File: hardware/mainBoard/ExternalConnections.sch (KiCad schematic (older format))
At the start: 8 parts

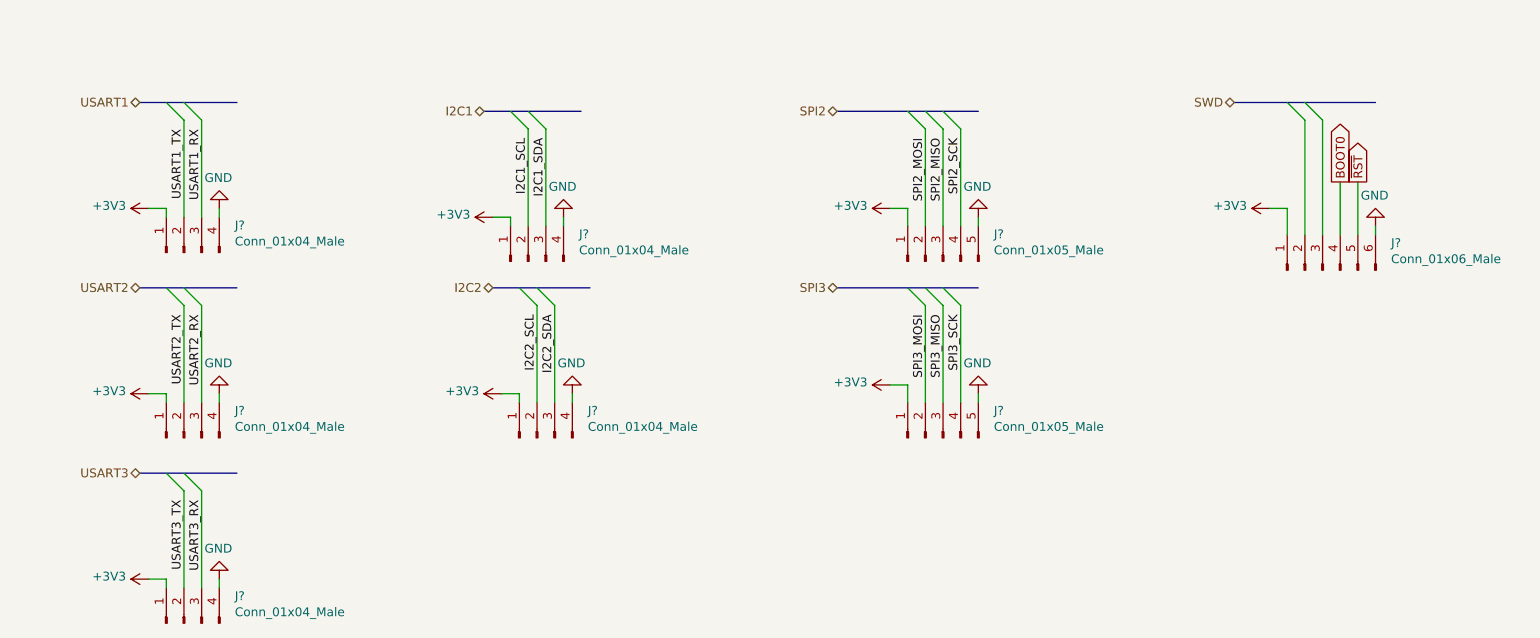
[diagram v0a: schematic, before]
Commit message: Ended schematic, created some pcb footprints
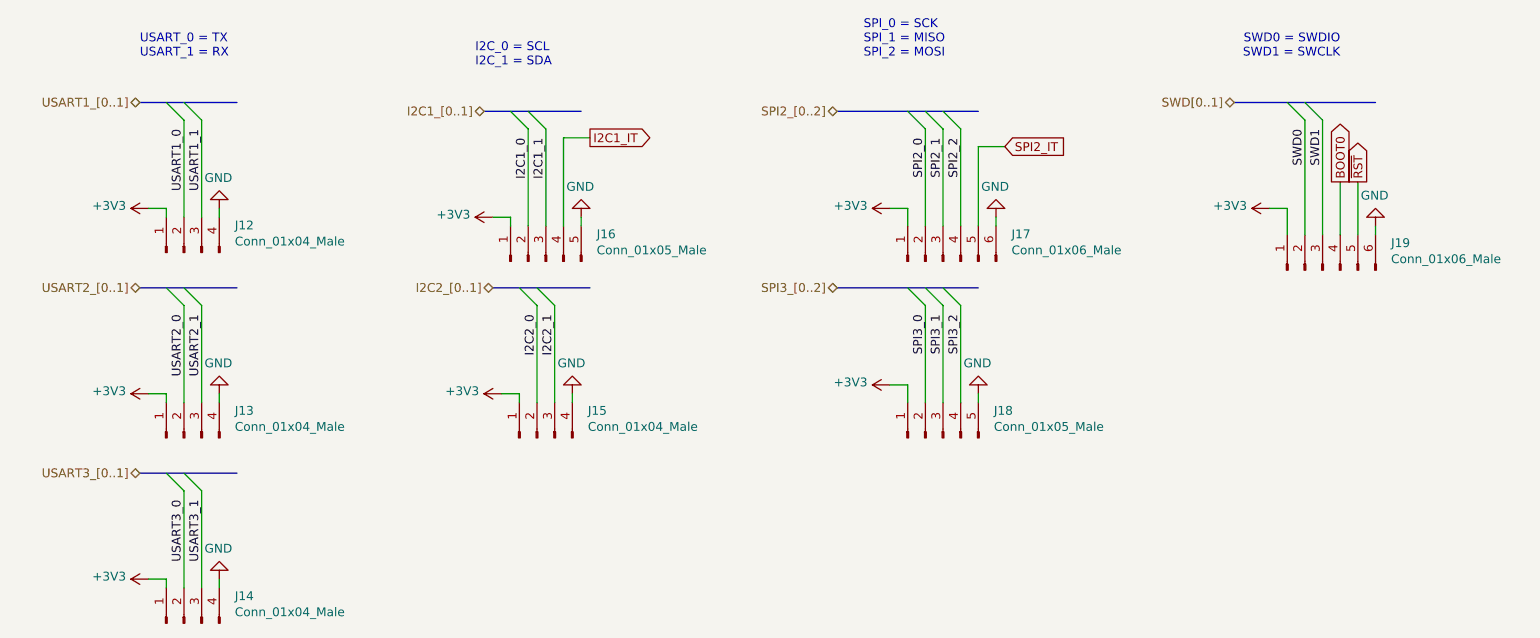
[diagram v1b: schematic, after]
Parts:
- removed J?: Conn_01x04_Male, symbol Connector:Conn_01x04_Male
- removed J?: Conn_01x05_Male, symbol Connector:Conn_01x05_Male
- added J16: Conn_01x05_Male, Connector_JST:JST_EH_B5B-EH-A_1x05_P2.50mm_Vertical, symbol Connector:Conn_01x05_Male
- added J17: Conn_01x06_Male, Connector_JST:JST_EH_B6B-EH-A_1x06_P2.50mm_Vertical, symbol Connector:Conn_01x06_Male
- J12, J13, J14, J15: renamed from J?; footprint (none) -> Connector_JST:JST_EH_B4B-EH-A_1x04_P2.50mm_Vertical
- J18: renamed from J?; footprint (none) -> Connector_JST:JST_EH_B5B-EH-A_1x05_P2.50mm_Vertical
- J19: renamed from J?; footprint (none) -> Connector_JST:JST_EH_B6B-EH-A_1x06_P2.50mm_Vertical
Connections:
- net +3V3: now also J16.1 (Pin_1), J17.1 (Pin_1)
- net GND: now also J16.5 (Pin_5), J17.6 (Pin_6)
- net SWD0: now reaches J19.2 (Pin_2)
- net SWD1: now reaches J19.3 (Pin_3)
- net I2C2_SCL renamed I2C2_0
- net I2C2_SDA renamed I2C2_1
- net SPI3_MISO renamed SPI3_1
- net SPI3_MOSI renamed SPI3_0
- net SPI3_SCK renamed SPI3_2
- net USART1_RX renamed USART1_1
- net USART1_TX renamed USART1_0
- net USART2_RX renamed USART2_1
- net USART2_TX renamed USART2_0
- net USART3_RX renamed USART3_1
- net USART3_TX renamed USART3_0
- new net I2C1_0: J16.2 (Pin_2)
- new net I2C1_1: J16.3 (Pin_3)
- new net I2C1_IT: J16.4 (Pin_4)
- new net SPI2_0: J17.2 (Pin_2)
- new net SPI2_1: J17.3 (Pin_3)
- new net SPI2_2: J17.4 (Pin_4)
- new net SPI2_IT: J17.5 (Pin_5)
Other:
- note added: "I2C_0 = SCL\nI2C_1 = SDA"
- note added: "SPI_0 = SCK\nSPI_1 = MISO\nSPI_2 = MOSI"
- note added: "SWD0 = SWDIO\nSWD1 = SWCLK"
- note added: "USART_0 = TX\nUSART_1 = RX"
